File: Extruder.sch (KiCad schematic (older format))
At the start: 2 parts, among them J10 Probe, J11 Extruder Heater

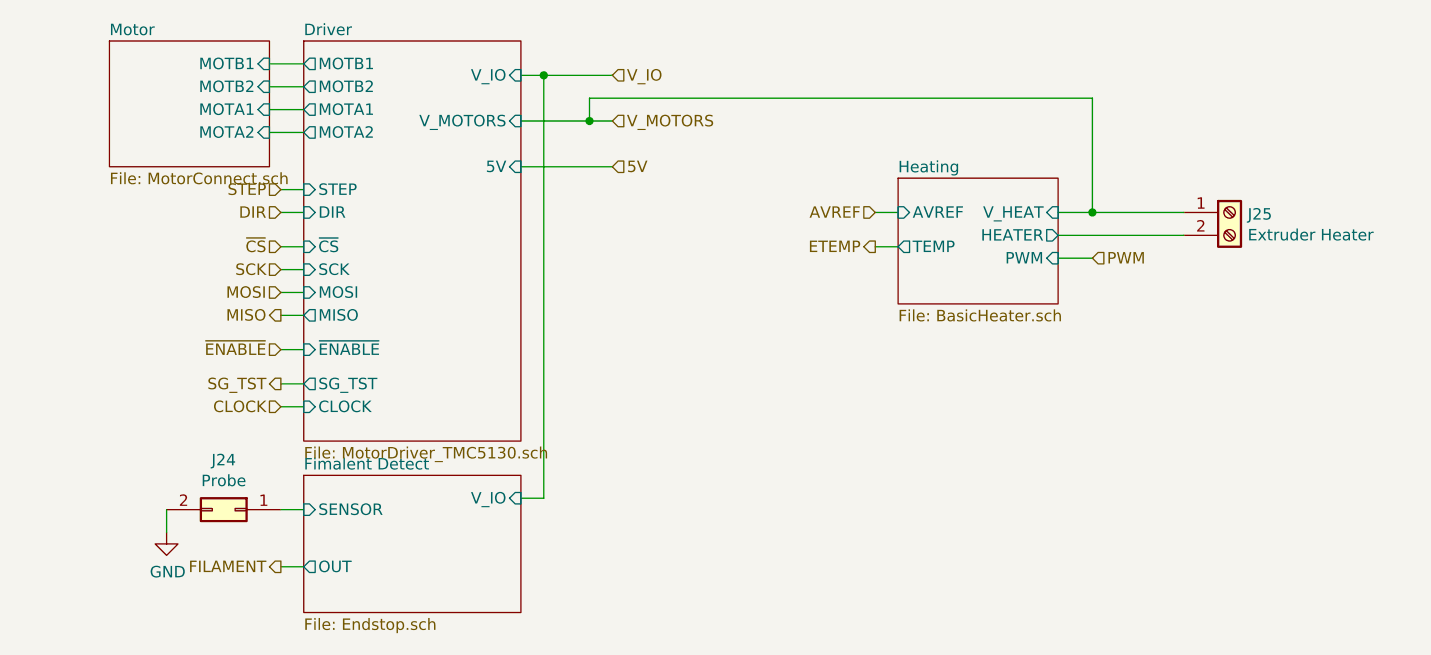
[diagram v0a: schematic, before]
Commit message: Reset schematics for tmc2660. Clean the board layout.
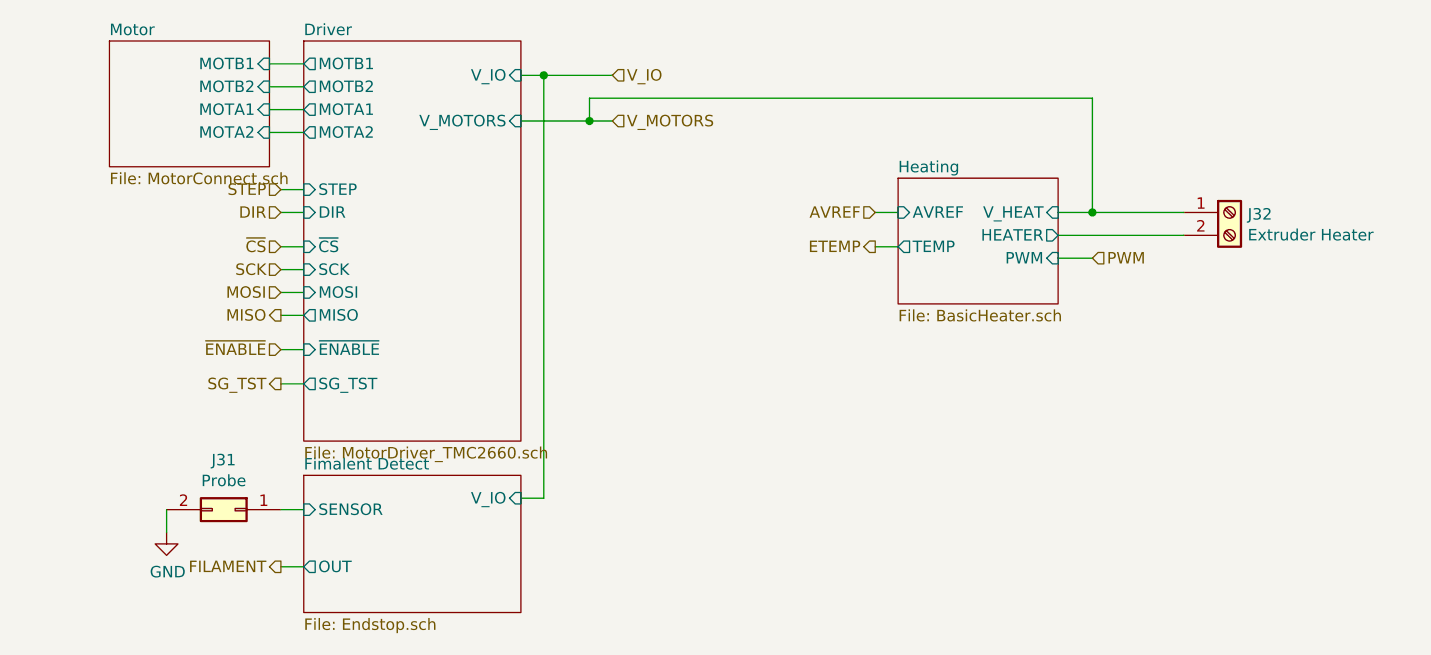
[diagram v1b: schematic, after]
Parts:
- renumbered J10 to J17, J11 to J18
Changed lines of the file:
@@
 U 5AD4B0F5
 F0 "Driver" 50
-F1 "MotorDriver_TMC5130.sch" 50
+F1 "MotorDriver_TMC2660.sch" 50
 F2 "V_IO" I R 3650 2100 50
 F3 "V_MOTORS" I R 3650 2300 50
@@
 F10 "~ENABLE" I L 2700 3300 50
 F11 "SG_TST" O L 2700 3450 50
-F12 "5V" I R 3650 2500 50
-F13 "CLOCK" I L 2700 3550 50
-F14 "MOTB1" O L 2700 2050 50
-F15 "MOTA1" O L 2700 2250 50
-F16 "MOTA2" O L 2700 2350 50
-F17 "MOTB2" O L 2700 2150 50
+F12 "MOTB1" O L 2700 2050 50
+F13 "MOTA1" O L 2700 2250 50
+F14 "MOTA2" O L 2700 2350 50
+F15 "MOTB2" O L 2700 2150 50
 $EndSheet
 Text HLabel 2600 2600 0    50   Input ~ 0
@@
 	2600 4250 2700 4250
 $Comp
-L Connector_Generic:Conn_02x01 J10
+L Connector_Generic:Conn_02x01 J17
 U 1 1 5AD4BF35
 P 2400 4000
-AR Path="/5AC337B6/5ACBE919/5AD4BF35" Ref="J10"  Part="1"
-AR Path="/5AC337B6/5AD9F95A/5AD4BF35" Ref="J24"  Part="1"
-F 0 "J24" H 2450 4217 50  0000 C CNN
+AR Path="/5AC337B6/5ACBE919/5AD4BF35" Ref="J17"  Part="1"
+AR Path="/5AC337B6/5AD9F95A/5AD4BF35" Ref="J31"  Part="1"
+F 0 "J31" H 2450 4217 50  0000 C CNN
 F 1 "Probe" H 2450 4126 50  0000 C CNN
 F 2 "Connector_PinHeader_2.54mm:PinHeader_1x02_P2.54mm_Vertical" H 2400 4000 50  0001 C CNN
@@
 	2600 4000 2700 4000
 $Comp
-L power:GND #PWR011
+L power:GND #PWR022
 U 1 1 5AD4C143
 P 2100 4100
-AR Path="/5AC337B6/5ACBE919/5AD4C143" Ref="#PWR011"  Part="1"
-AR Path="/5AC337B6/5AD9F95A/5AD4C143" Ref="#PWR056"  Part="1"
-F 0 "#PWR056" H 2100 3850 50  0001 C CNN
+AR Path="/5AC337B6/5ACBE919/5AD4C143" Ref="#PWR022"  Part="1"
+AR Path="/5AC337B6/5AD9F95A/5AD4C143" Ref="#PWR067"  Part="1"
+F 0 "#PWR067" H 2100 3850 50  0001 C CNN
 F 1 "GND" H 2105 3927 50  0000 C CNN
 F 2 "" H 2100 4100 50  0001 C CNN
@@
 	6000 2900 6150 2900
 $Comp
-L PrntrBoardV1-rescue:Screw_Terminal_01x02-Connector_Specialized J11
+L PrntrBoardV1-rescue:Screw_Terminal_01x02-Connector_Specialized J18
 U 1 1 5AD53BDD
 P 6750 2700
-AR Path="/5AC337B6/5ACBE919/5AD53BDD" Ref="J11"  Part="1"
-AR Path="/5AC337B6/5AD9F95A/5AD53BDD" Ref="J25"  Part="1"
-F 0 "J25" H 6829 2692 50  0000 L CNN
+AR Path="/5AC337B6/5ACBE919/5AD53BDD" Ref="J18"  Part="1"
+AR Path="/5AC337B6/5AD9F95A/5AD53BDD" Ref="J32"  Part="1"
+F 0 "J32" H 6829 2692 50  0000 L CNN
 F 1 "Extruder Heater" H 6829 2601 50  0000 L CNN
 F 2 "PrntrBoardV1:TerminalBlock_Phoenix_PT-1,5-2-3.5-H_1x02_P3.50mm_Horizontal" H 6750 2700 50  0001 C CNN
@@
 	6550 2700 6150 2700
 Connection ~ 6150 2700
-Text HLabel 4050 2500 2    50   Input ~ 0
-5V
-Wire Wire Line
-	4050 2500 3650 2500
-Text HLabel 2600 3550 0    50   Input ~ 0
-CLOCK
-Wire Wire Line
-	2600 3550 2700 3550
 $EndSCHEMATC

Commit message: Flip the top row power connectors - they were facing the worng way.
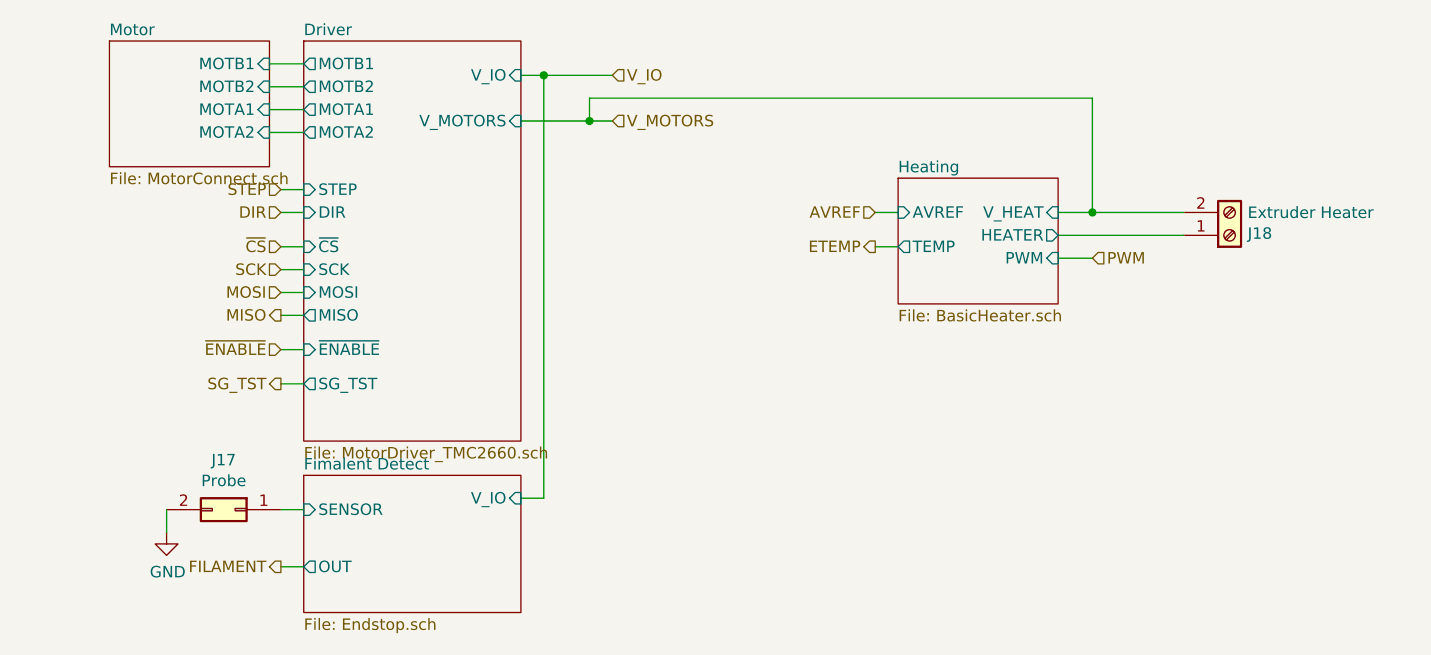
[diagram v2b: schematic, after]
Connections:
- net Heating/HEATER: now also J18.1 (Pin_1); no longer J18.2 (Pin_2)
- net V_MOTORS: now also J18.2 (Pin_2); no longer J18.1 (Pin_1)
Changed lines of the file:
@@
-EESchema Schematic File Version 4
+EESchema Schematic File Version 5
 LIBS:PrntrBoardV1-cache
 EELAYER 29 0
@@
 AR Path="/5AC337B6/5ACBE919/5AD4BF35" Ref="J17"  Part="1"
 AR Path="/5AC337B6/5AD9F95A/5AD4BF35" Ref="J31"  Part="1"
-F 0 "J31" H 2450 4217 50  0000 C CNN
+F 0 "J17" H 2450 4217 50  0000 C CNN
 F 1 "Probe" H 2450 4126 50  0000 C CNN
 F 2 "Connector_PinHeader_2.54mm:PinHeader_1x02_P2.54mm_Vertical" H 2400 4000 50  0001 C CNN
@@
 AR Path="/5AC337B6/5ACBE919/5AD4C143" Ref="#PWR022"  Part="1"
 AR Path="/5AC337B6/5AD9F95A/5AD4C143" Ref="#PWR067"  Part="1"
-F 0 "#PWR067" H 2100 3850 50  0001 C CNN
+F 0 "#PWR022" H 2100 3850 50  0001 C CNN
 F 1 "GND" H 2105 3927 50  0000 C CNN
 F 2 "" H 2100 4100 50  0001 C CNN
@@
 L PrntrBoardV1-rescue:Screw_Terminal_01x02-Connector_Specialized J18
 U 1 1 5AD53BDD
-P 6750 2700
+P 6750 2800
 AR Path="/5AC337B6/5ACBE919/5AD53BDD" Ref="J18"  Part="1"
 AR Path="/5AC337B6/5AD9F95A/5AD53BDD" Ref="J32"  Part="1"
-F 0 "J32" H 6829 2692 50  0000 L CNN
-F 1 "Extruder Heater" H 6829 2601 50  0000 L CNN
-F 2 "PrntrBoardV1:TerminalBlock_Phoenix_PT-1,5-2-3.5-H_1x02_P3.50mm_Horizontal" H 6750 2700 50  0001 C CNN
-F 3 "~" H 6750 2700 50  0001 C CNN
-	1    6750 2700
-	1    0    0    -1
+F 0 "J18" H 6829 2792 50  0000 L CNN
+F 1 "Extruder Heater" H 6829 2701 50  0000 L CNN
+F 2 "PrntrBoardV1:TerminalBlock_Phoenix_PT-1,5-2-3.5-H_1x02_P3.50mm_Horizontal" H 6750 2800 50  0001 C CNN
+F 3 "~" H 6750 2800 50  0001 C CNN
+	1    6750 2800
+	1    0    0    1
 $EndComp
 Wire Wire Line

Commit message: Added reverse polarity input protection diodes. Re-routed input power.
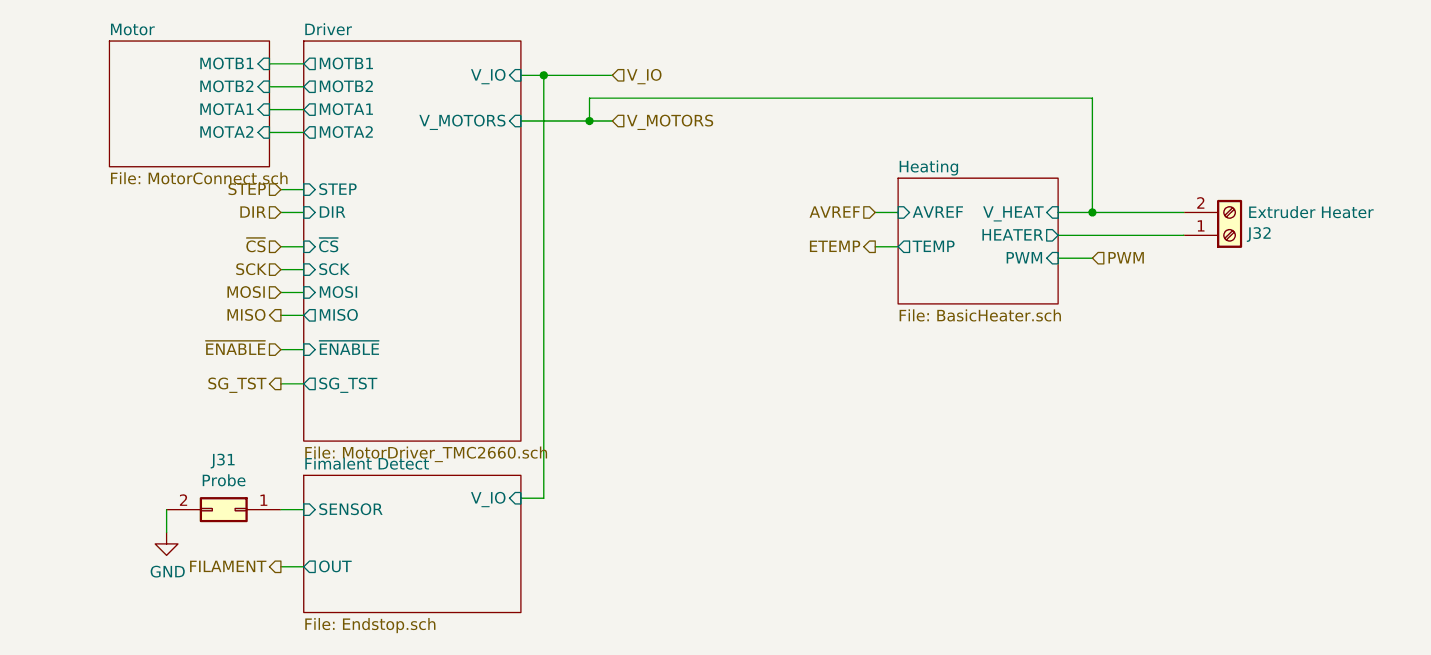
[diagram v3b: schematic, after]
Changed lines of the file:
@@
 AR Path="/5AC337B6/5ACBE919/5AD4BF35" Ref="J17"  Part="1"
 AR Path="/5AC337B6/5AD9F95A/5AD4BF35" Ref="J31"  Part="1"
-F 0 "J17" H 2450 4217 50  0000 C CNN
+F 0 "J31" H 2450 4217 50  0000 C CNN
 F 1 "Probe" H 2450 4126 50  0000 C CNN
 F 2 "Connector_PinHeader_2.54mm:PinHeader_1x02_P2.54mm_Vertical" H 2400 4000 50  0001 C CNN
@@
 AR Path="/5AC337B6/5ACBE919/5AD4C143" Ref="#PWR022"  Part="1"
 AR Path="/5AC337B6/5AD9F95A/5AD4C143" Ref="#PWR067"  Part="1"
-F 0 "#PWR022" H 2100 3850 50  0001 C CNN
+F 0 "#PWR067" H 2100 3850 50  0001 C CNN
 F 1 "GND" H 2105 3927 50  0000 C CNN
 F 2 "" H 2100 4100 50  0001 C CNN
@@
 AR Path="/5AC337B6/5ACBE919/5AD53BDD" Ref="J18"  Part="1"
 AR Path="/5AC337B6/5AD9F95A/5AD53BDD" Ref="J32"  Part="1"
-F 0 "J18" H 6829 2792 50  0000 L CNN
+F 0 "J32" H 6829 2792 50  0000 L CNN
 F 1 "Extruder Heater" H 6829 2701 50  0000 L CNN
 F 2 "PrntrBoardV1:TerminalBlock_Phoenix_PT-1,5-2-3.5-H_1x02_P3.50mm_Horizontal" H 6750 2800 50  0001 C CNN

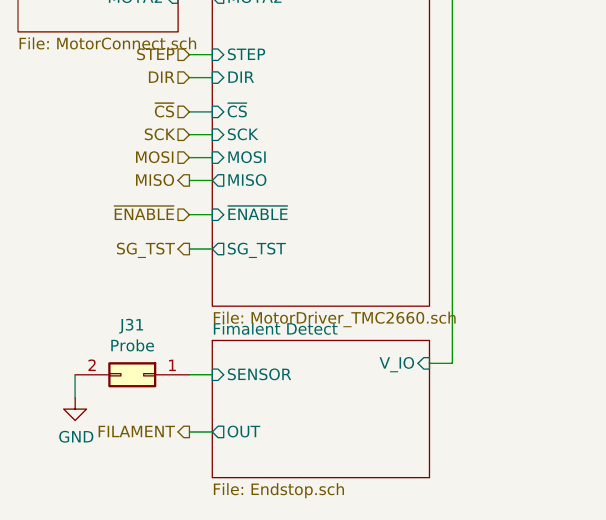
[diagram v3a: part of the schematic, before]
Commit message: Added clock source for the TMC2660 drivers.
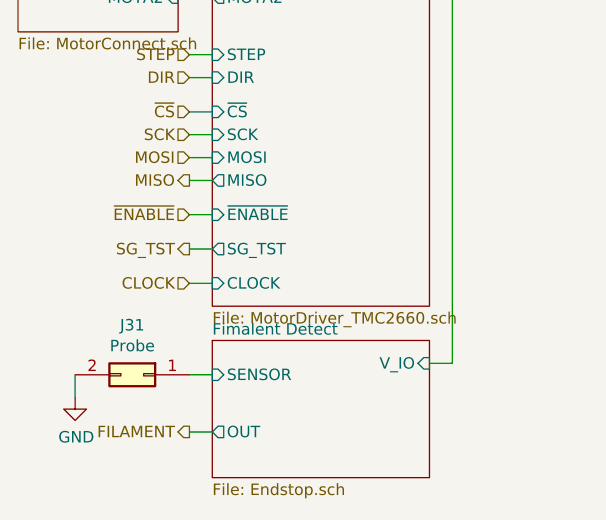
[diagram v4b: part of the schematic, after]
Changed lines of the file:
@@
 F14 "MOTA2" O L 2700 2350 50
 F15 "MOTB2" O L 2700 2150 50
+F16 "CLOCK" I L 2700 3600 50
 $EndSheet
 Text HLabel 2600 2600 0    50   Input ~ 0
@@
 	6550 2700 6150 2700
 Connection ~ 6150 2700
+Text HLabel 2600 3600 0    50   Input ~ 0
+CLOCK
+Wire Wire Line
+	2700 3600 2600 3600
 $EndSCHEMATC

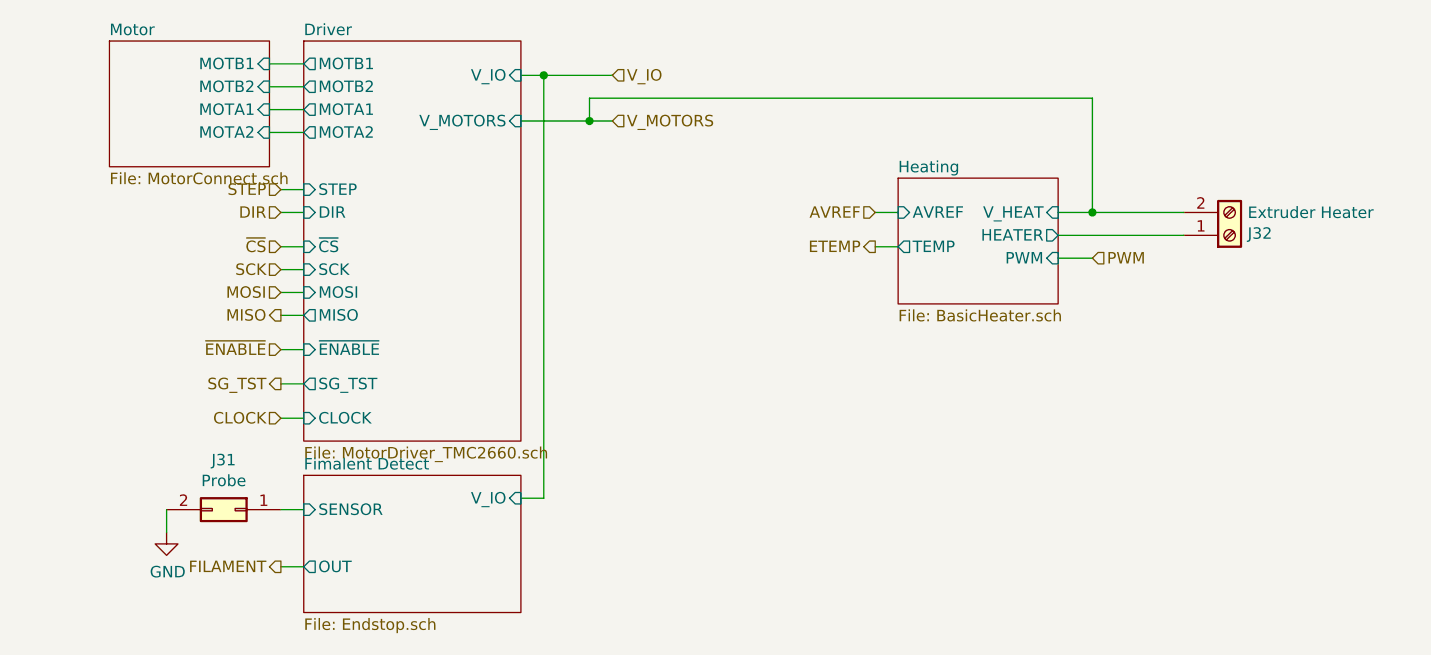
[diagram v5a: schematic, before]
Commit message: Wired most of the schematics for 2209 drivers.
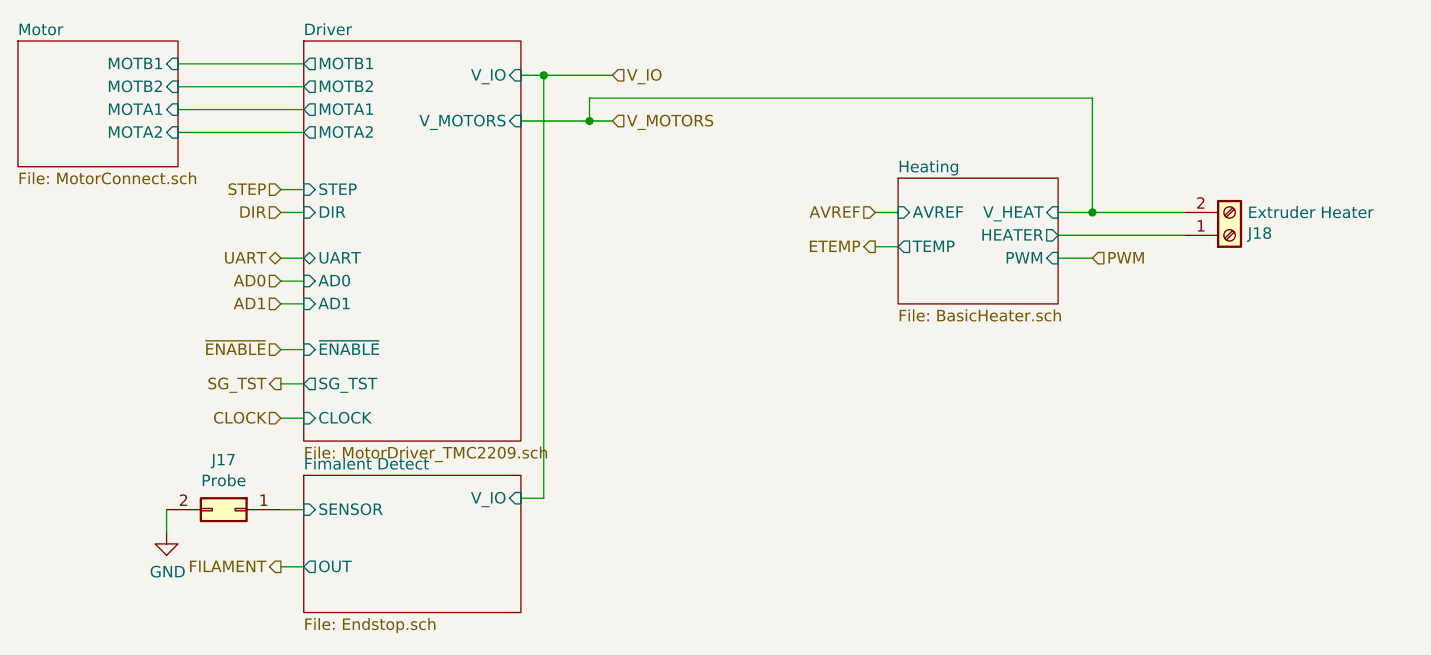
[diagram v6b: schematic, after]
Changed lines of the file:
@@
 $Descr A4 11693 8268
 encoding utf-8
-Sheet 25 35
+Sheet 3 35
 Title ""
 Date ""
@@
 U 5AD4B0F5
 F0 "Driver" 50
-F1 "MotorDriver_TMC2660.sch" 50
+F1 "MotorDriver_TMC2209.sch" 50
 F2 "V_IO" I R 3650 2100 50
 F3 "V_MOTORS" I R 3650 2300 50
 F4 "STEP" I L 2700 2600 50
 F5 "DIR" I L 2700 2700 50
-F6 "~CS" I L 2700 2850 50
-F7 "SCK" I L 2700 2950 50
-F8 "MOSI" I L 2700 3050 50
-F9 "MISO" O L 2700 3150 50
-F10 "~ENABLE" I L 2700 3300 50
-F11 "SG_TST" O L 2700 3450 50
-F12 "MOTB1" O L 2700 2050 50
-F13 "MOTA1" O L 2700 2250 50
-F14 "MOTA2" O L 2700 2350 50
-F15 "MOTB2" O L 2700 2150 50
-F16 "CLOCK" I L 2700 3600 50
+F6 "~ENABLE" I L 2700 3300 50
+F7 "SG_TST" O L 2700 3450 50
+F8 "MOTB1" O L 2700 2050 50
+F9 "MOTA1" O L 2700 2250 50
+F10 "MOTA2" O L 2700 2350 50
+F11 "MOTB2" O L 2700 2150 50
+F12 "CLOCK" I L 2700 3600 50
+F13 "UART" B L 2700 2900 50
+F14 "AD0" I L 2700 3000 50
+F15 "AD1" I L 2700 3100 50
 $EndSheet
 Text HLabel 2600 2600 0    50   Input ~ 0
@@
 Text HLabel 2600 2700 0    50   Input ~ 0
 DIR
-Text HLabel 2600 2850 0    50   Input ~ 0
-~CS
-Text HLabel 2600 2950 0    50   Input ~ 0
-SCK
-Text HLabel 2600 3050 0    50   Input ~ 0
-MOSI
-Text HLabel 2600 3150 0    50   Output ~ 0
-MISO
 Text HLabel 2600 3300 0    50   Input ~ 0
 ~ENABLE
@@
 Wire Wire Line
 	2700 2700 2600 2700
-Wire Wire Line
-	2700 2850 2600 2850
-Wire Wire Line
-	2700 2950 2600 2950
-Wire Wire Line
-	2700 3050 2600 3050
-Wire Wire Line
-	2700 3150 2600 3150
 Wire Wire Line
 	2700 3300 2600 3300
@@
 AR Path="/5AC337B6/5ACBE919/5AD4BF35" Ref="J17"  Part="1"
 AR Path="/5AC337B6/5AD9F95A/5AD4BF35" Ref="J31"  Part="1"
-F 0 "J31" H 2450 4217 50  0000 C CNN
+F 0 "J17" H 2450 4217 50  0000 C CNN
 F 1 "Probe" H 2450 4126 50  0000 C CNN
 F 2 "Connector_PinHeader_2.54mm:PinHeader_1x02_P2.54mm_Vertical" H 2400 4000 50  0001 C CNN
@@
 AR Path="/5AC337B6/5ACBE919/5AD4C143" Ref="#PWR022"  Part="1"
 AR Path="/5AC337B6/5AD9F95A/5AD4C143" Ref="#PWR067"  Part="1"
-F 0 "#PWR067" H 2100 3850 50  0001 C CNN
+F 0 "#PWR022" H 2100 3850 50  0001 C CNN
 F 1 "GND" H 2105 3927 50  0000 C CNN
 F 2 "" H 2100 4100 50  0001 C CNN
@@
 	2100 4100 2100 4000
 $Sheet
-S 1850 1950 700  550
+S 1450 1950 700  550
 U 5AD4C411
 F0 "Motor" 50
 F1 "MotorConnect.sch" 50
-F2 "MOTB1" I R 2550 2050 50
-F3 "MOTB2" I R 2550 2150 50
-F4 "MOTA2" I R 2550 2350 50
-F5 "MOTA1" I R 2550 2250 50
+F2 "MOTB1" I R 2150 2050 50
+F3 "MOTB2" I R 2150 2150 50
+F4 "MOTA2" I R 2150 2350 50
+F5 "MOTA1" I R 2150 2250 50
 $EndSheet
-Wire Wire Line
-	2550 2050 2700 2050
-Wire Wire Line
-	2700 2150 2550 2150
-Wire Wire Line
-	2700 2250 2550 2250
-Wire Wire Line
-	2700 2350 2550 2350
 $Sheet
 S 5300 2550 700  550
@@
 AR Path="/5AC337B6/5ACBE919/5AD53BDD" Ref="J18"  Part="1"
 AR Path="/5AC337B6/5AD9F95A/5AD53BDD" Ref="J32"  Part="1"
-F 0 "J32" H 6829 2792 50  0000 L CNN
+F 0 "J18" H 6829 2792 50  0000 L CNN
 F 1 "Extruder Heater" H 6829 2701 50  0000 L CNN
 F 2 "PrntrBoardV1:TerminalBlock_Phoenix_PT-1,5-2-3.5-H_1x02_P3.50mm_Horizontal" H 6750 2800 50  0001 C CNN
@@
 Wire Wire Line
 	2700 3600 2600 3600
+Wire Wire Line
+	2150 2350 2700 2350
+Wire Wire Line
+	2150 2250 2700 2250
+Wire Wire Line
+	2150 2150 2700 2150
+Wire Wire Line
+	2150 2050 2700 2050
+Text HLabel 2600 2900 0    50   BiDi ~ 0
+UART
+Text HLabel 2600 3000 0    50   Input ~ 0
+AD0
+Text HLabel 2600 3100 0    50   Input ~ 0
+AD1
+Wire Wire Line
+	2600 3100 2700 3100
+Wire Wire Line
+	2600 3000 2700 3000
+Wire Wire Line
+	2600 2900 2700 2900
 $EndSCHEMATC
